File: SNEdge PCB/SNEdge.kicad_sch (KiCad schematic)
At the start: 40 parts, among them J1 RGB_OUT, U1 THS7376

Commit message: Prepping for release
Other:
- company: (none) -> Thunder Technologies
- title: (none) -> SNEdge
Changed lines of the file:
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@@
 	(generator_version "8.0")
 	(paper "A4")
+	(title_block
+		(title "SNEdge")
+		(date "2024-08-31")
+		(rev "1")
+		(company "Thunder Technologies")
+		(comment 1 "Designed By InnocuousMuffin")
+		(comment 2 "Design based on YoshiYukiBlade's work")
+	)
 	(junction
 		(at 115.57 49.53)

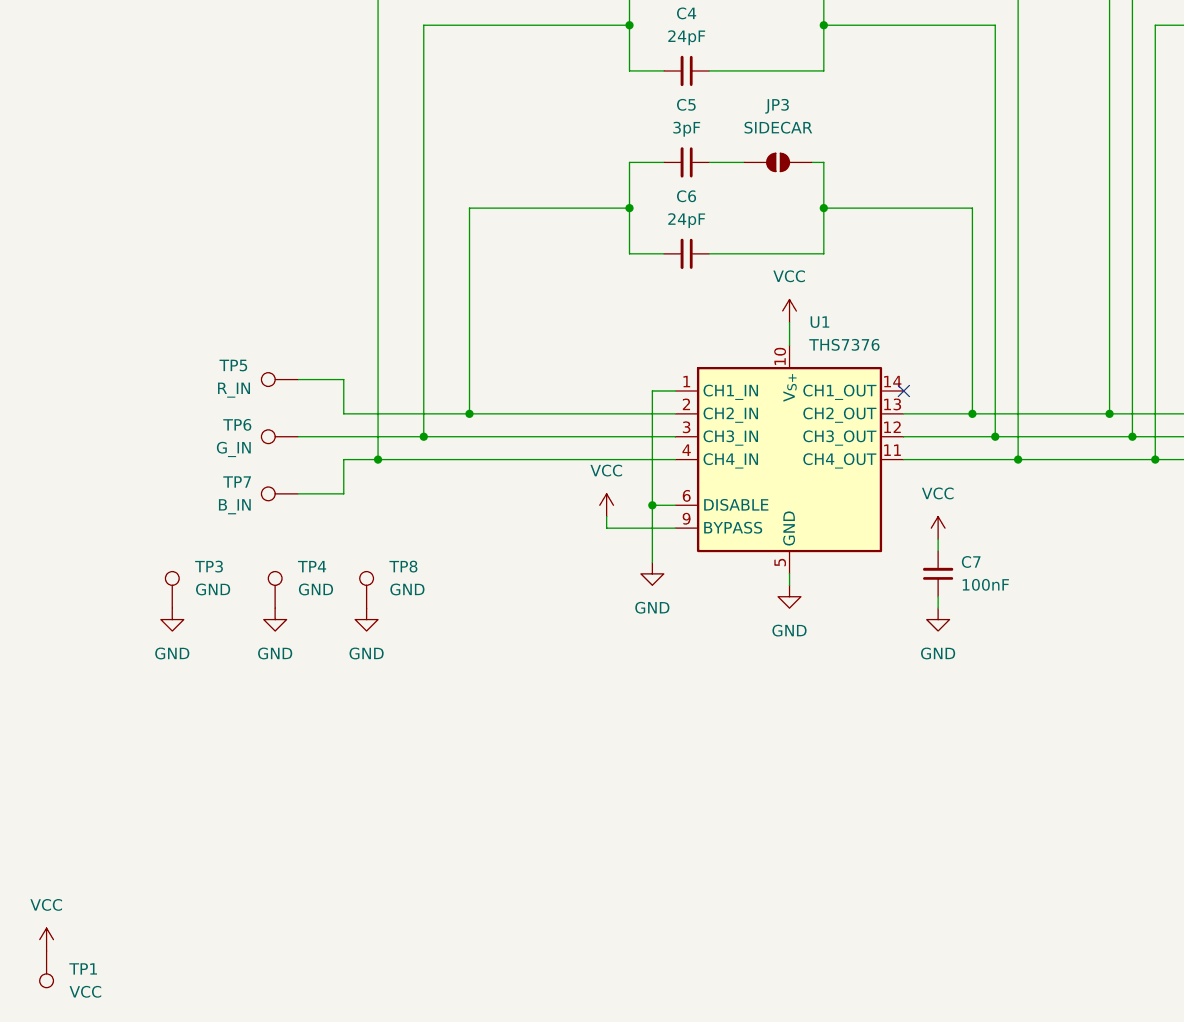
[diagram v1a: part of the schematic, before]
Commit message: AC coupled input, SD filter enabled
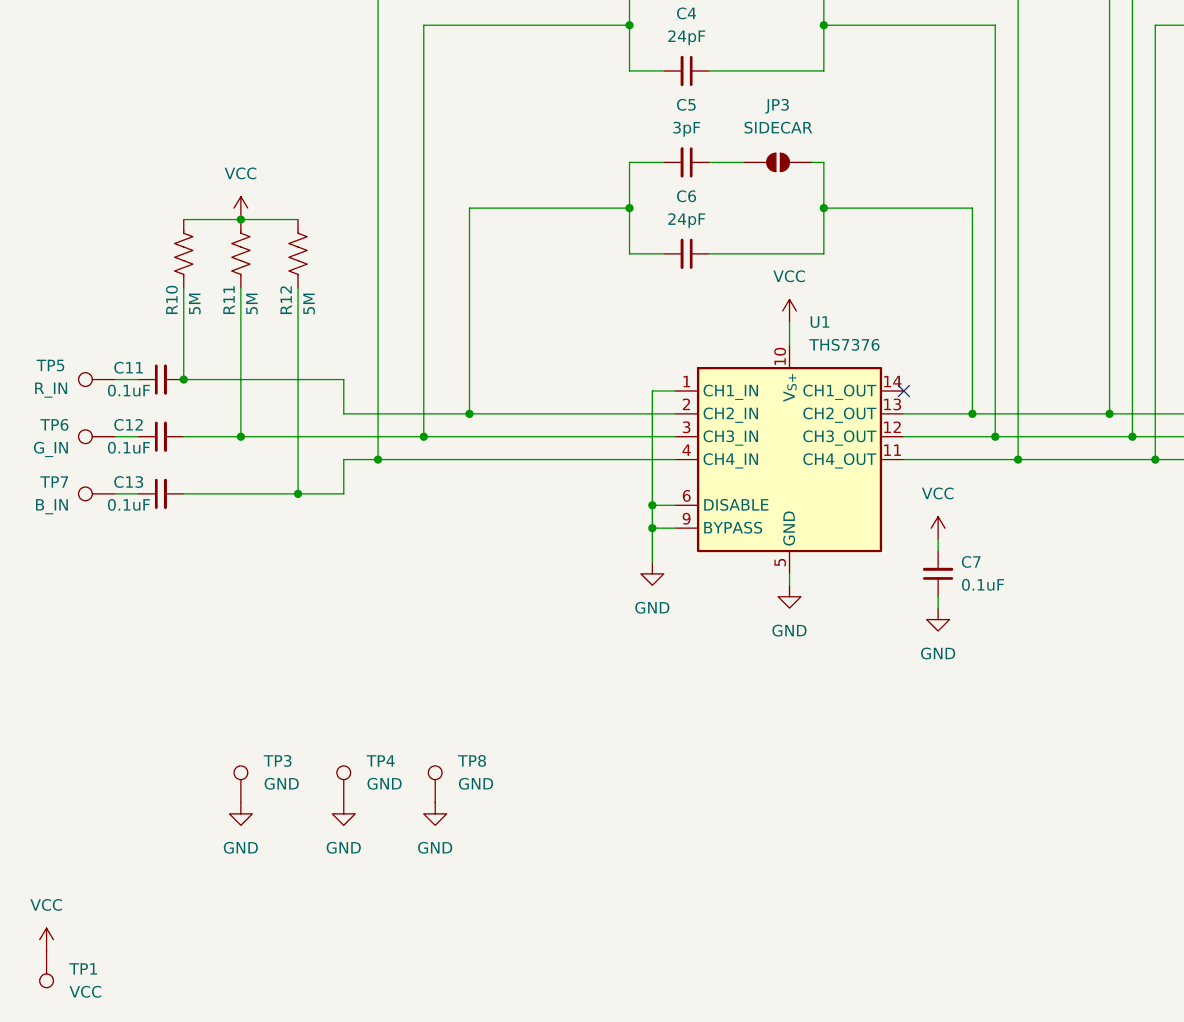
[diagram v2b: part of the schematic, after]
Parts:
- added C11, C12, C13: 0.1uF, Capacitor_SMD:C_0805_2012Metric, symbol Device:C_Small
- added R10, R11, R12: 5M, Resistor_SMD:R_0805_2012Metric, symbol Device:R_US
- C7: value 100nF -> 0.1uF
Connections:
- net GND: now also U1.9 (BYPASS)
- net VCC: now also R10.1, R11.1, R12.1; no longer U1.9 (BYPASS)
- net at C5.2, C6.2, U1.2 (CH2_IN): now also C11.2, R10.2; no longer TP5.1
- net at C3.2, C4.2, U1.3 (CH3_IN): now also C12.2, R11.2; no longer TP6.1
- net at C1.2, C2.2, U1.4 (CH4_IN): now also C13.2, R12.2; no longer TP7.1
- new net: C13.1, TP7.1
- new net: C11.1, TP5.1
- new net: C12.1, TP6.1
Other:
- moved on the sheet: TP3, TP4, TP5, TP6, TP7, TP8
